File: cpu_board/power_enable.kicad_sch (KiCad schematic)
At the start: 7 parts

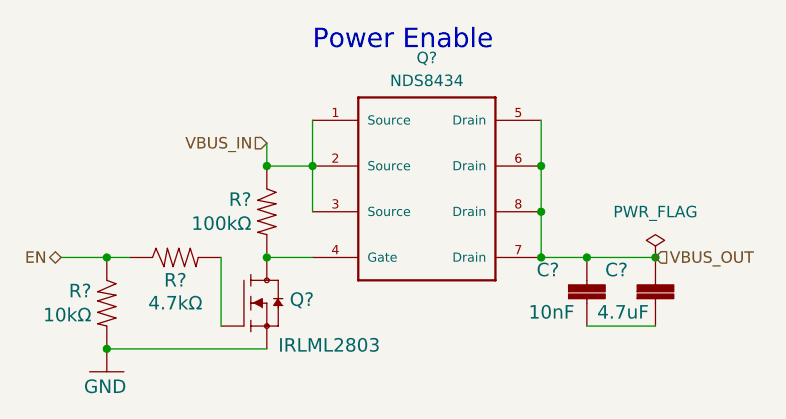
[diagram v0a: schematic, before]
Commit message: route most of power distribution
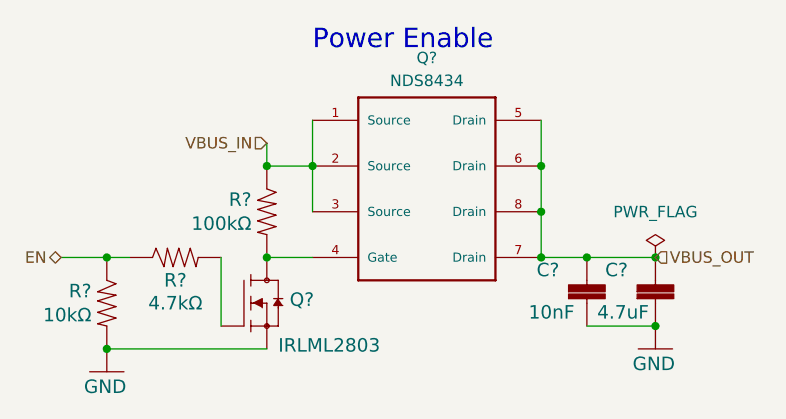
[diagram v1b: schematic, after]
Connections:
- net GND: now also C?.2, C?.2
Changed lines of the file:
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@@
   (junction (at 113.665 95.25) (diameter 0) (color 0 0 0 0)
+  )
+  (junction (at 174.625 102.87) (diameter 0) (color 0 0 0 0)
   )
   (junction (at 161.925 90.17) (diameter 0) (color 0 0 0 0)
@@
       (project "cpu_board"
         (path "/c4fd7bdd-408e-44be-b66f-e6a18a0ca6e3/cea27ea3-b252-471b-8ae3-89651d2bf5e1/fef67fc1-8026-4168-9599-05f275dfb457"
-          (reference "R43") (unit 1)
+          (reference "R36") (unit 1)
         )
       )
@@
       (project "cpu_board"
         (path "/c4fd7bdd-408e-44be-b66f-e6a18a0ca6e3/cea27ea3-b252-471b-8ae3-89651d2bf5e1/fef67fc1-8026-4168-9599-05f275dfb457"
-          (reference "#GND09") (unit 1)
+          (reference "#GND010") (unit 1)
         )
       )
@@
       (project "cpu_board"
         (path "/c4fd7bdd-408e-44be-b66f-e6a18a0ca6e3/cea27ea3-b252-471b-8ae3-89651d2bf5e1/fef67fc1-8026-4168-9599-05f275dfb457"
-          (reference "R42") (unit 1)
+          (reference "R35") (unit 1)
         )
       )
@@
       (project "cpu_board"
         (path "/c4fd7bdd-408e-44be-b66f-e6a18a0ca6e3/cea27ea3-b252-471b-8ae3-89651d2bf5e1/fef67fc1-8026-4168-9599-05f275dfb457"
-          (reference "R41") (unit 1)
+          (reference "R34") (unit 1)
         )
       )
@@
         )
       )
+    )
+  )
+  (symbol (lib_id "mainboard:GND") (at 174.625 105.41 0) (unit 1)
+    (in_bom yes) (on_board yes) (dnp no)
+    (property "Reference" "#GND?" (at 174.625 105.41 0)
+      (effects (font (size 1.27 1.27)) hide)
+    )
+    (property "Value" "GND" (at 172.085 107.95 0)
+      (effects (font (size 1.4986 1.4986)) (justify left bottom))
+    )
+    (property "Footprint" "" (at 174.625 105.41 0)
+      (effects (font (size 1.27 1.27)) hide)
+    )
+    (property "Datasheet" "" (at 174.625 105.41 0)
+      (effects (font (size 1.27 1.27)) hide)
+    )
+    (pin "1")
+    (instances
+      (project "adcs-hardware"
+        (path "/2bf29f96-8e90-4c56-8856-49bc3b5fab50/96c1dca3-3491-4490-97b2-299dd5a0d462"
+          (reference "#GND?") (unit 1)
+        )
+        (path "/2bf29f96-8e90-4c56-8856-49bc3b5fab50/2011b62c-b542-4899-89c4-f1a49629fe42"
+          (reference "#GND?") (unit 1)
+        )
+        (path "/2bf29f96-8e90-4c56-8856-49bc3b5fab50/dbac343c-e1e8-4f27-95db-48905ebe6ac8"
+          (reference "#GND?") (unit 1)
+        )
+        (path "/2bf29f96-8e90-4c56-8856-49bc3b5fab50/96c1dca3-3491-4490-97b2-299dd5a0d462/050cb11f-ff11-499c-a248-6fb9f1092987"
+          (reference "#GND?") (unit 1)
+        )
+        (path "/2bf29f96-8e90-4c56-8856-49bc3b5fab50/2011b62c-b542-4899-89c4-f1a49629fe42/050cb11f-ff11-499c-a248-6fb9f1092987"
+          (reference "#GND?") (unit 1)
+        )
+        (path "/2bf29f96-8e90-4c56-8856-49bc3b5fab50/1539ef5d-4f4f-4a9e-ae0a-b29bdc9f46f8/d7510623-5924-4e82-97b6-641ec54de302"
+          (reference "#GND?") (unit 1)
+        )
+        (path "/2bf29f96-8e90-4c56-8856-49bc3b5fab50/e6d989e1-3d58-4abb-9f22-cf061fe5e0a3"
+          (reference "#GND?") (unit 1)
+        )
+        (path "/2bf29f96-8e90-4c56-8856-49bc3b5fab50/09e775d0-de49-4fe2-956d-adceee72ccf4"
+          (reference "#GND?") (unit 1)
+        )
+      )
+      (project "cpu_board"
+        (path "/c4fd7bdd-408e-44be-b66f-e6a18a0ca6e3/cea27ea3-b252-471b-8ae3-89651d2bf5e1/fef67fc1-8026-4168-9599-05f275dfb457"
+          (reference "#GND011") (unit 1)
+        )
+      )
+      (project "mainboard"
+        (path "/db20b18b-d25a-428e-8229-70a189e1de75/00000000-0000-0000-0000-00005cec5dde"
+          (reference "#GND?") (unit 1)
+        )
+      )

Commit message: continue work on fanout
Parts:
- C?: footprint Capacitor_SMD:C_0402_1005Metric -> adcs:Perfect_0402
- C?: footprint Capacitor_SMD:C_0402_1005Metric -> adcs:Perfect_0201
- R? (x3): footprint Resistor_SMD:R_0402_1005Metric -> adcs:Perfect_0402
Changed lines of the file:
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@@
       (effects (font (size 1.4986 1.4986)) (justify right))
     )
-    (property "Footprint" "Resistor_SMD:R_0402_1005Metric" (at 131.445 90.17 0)
+    (property "Footprint" "adcs:Perfect_0402" (at 131.445 90.17 0)
       (effects (font (size 1.27 1.27)) hide)
     )
@@
       (effects (font (size 1.4986 1.4986)) (justify left))
     )
-    (property "Footprint" "Capacitor_SMD:C_0402_1005Metric" (at 174.625 100.33 0)
+    (property "Footprint" "adcs:Perfect_0402" (at 174.625 100.33 0)
       (effects (font (size 1.27 1.27)) hide)
     )
@@
       (effects (font (size 1.4986 1.4986)))
     )
-    (property "Footprint" "Resistor_SMD:R_0402_1005Metric" (at 121.285 95.25 0)
+    (property "Footprint" "adcs:Perfect_0402" (at 121.285 95.25 0)
       (effects (font (size 1.27 1.27)) hide)
     )
@@
       (effects (font (size 1.4986 1.4986)) (justify right))
     )
-    (property "Footprint" "Resistor_SMD:R_0402_1005Metric" (at 113.665 100.33 0)
+    (property "Footprint" "adcs:Perfect_0402" (at 113.665 100.33 0)
       (effects (font (size 1.27 1.27)) hide)
     )
@@
       (effects (font (size 1.4986 1.4986)) (justify left))
     )
-    (property "Footprint" "Capacitor_SMD:C_0402_1005Metric" (at 167.005 100.33 0)
-      (effects (font (size 1.27 1.27)) hide)
-    )
+    (property "Footprint" "adcs:Perfect_0201" (at 167.005 100.33 0)
+      (effects (font (size 1.27 1.27)) hide)
+    )
